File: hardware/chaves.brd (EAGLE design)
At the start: 100 x 100 mm, 80 parts, among them IC1 40106N

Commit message: all done except ground plane
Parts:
- removed E$1, E$2, E$3, E$4: (no value), holes:3,0
- removed R1, R2, R3, R4, R5, R6: 10k, adafruit:0204/7
- added IN1, IN2: WQP-PJ301M-12_JACK, MusicThingModular:WQP-PJ301M-12_JACK
- added JP6, JP7: (no value), adafruit:1X03-CLEANBIG
- added POT7, POT8: 10k, pot-alps:ALPS_POT_VERTICAL
- moved BJ 61.3 mm to (97.5, 15.0), turned to 180 degrees
- moved GJ 55.6 mm to (97.5, 19.5), turned to 180 degrees
- moved RJ 49.4 mm to (97.5, 24.5), turned to 180 degrees
- moved JHSYNC 45.6 mm to (97.5, 38.0)
- moved JVSYNC 43.9 mm to (97.5, 42.5)
- moved JGND 41.1 mm to (97.5, 29.0), turned to 90 degrees
- moved JVCC 35.1 mm to (97.5, 33.0), turned to 90 degrees
- moved JP2 32.3 mm to (71.5, 39.0)
- moved JP1 32.2 mm to (66.0, 39.0)
- moved IC1 14.3 mm to (66.5, 15.5), turned to 90 degrees
- moved C1 12.0 mm to (22.5, 87.0)
- moved C4 11.5 mm to (22.5, 72.0)
- moved C6 11.5 mm to (22.5, 58.0)
- moved C8 11.3 mm to (22.5, 45.0)
- moved C10 11.0 mm to (22.5, 30.5)
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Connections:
- removed net N$3 (its old number): C5.1, U$8.1
- removed net N$36: IC1.13, LDR2.1, POT6.P$1, POT6.P$2, U$12.2
- removed net N$6 (its old number): C6.1, U$9.3
- new net N$23: IN1.P$1_TIP, POT7.P$3
- new net N$46: C10.2, U$11.1
- new net N$47: C10.1, C11.1, IC1.11, POT5.P$1, POT5.P$2
- new net N$48: C11.2, U$11.3
- new net N$49: C13.2, U$12.3
- new net N$50: C12.2, U$12.1
- new net N$51: C12.1, C13.1, IC1.13, POT6.P$1, POT6.P$2
- net GND: now also IN1.P$3_SLEEVE, IN2.P$3_SLEEVE, POT7.P$1, POT8.P$1; no longer R1.1, R2.1, R3.1, R4.1, R5.1, R6.1
- net N$1: now also C1.2; no longer C2.1
- net N$10: now also C6.2, U$9.1; no longer C10.1, U$11.3
- net N$11: now also C7.2, U$9.3; no longer C13.1, U$12.1
- net N$12: now also JP6.1, JP6.2, JP6.3, POT7.P$2; no longer C12.1, U$12.3
- net N$18: no longer R1.2
- net N$19: now also LDR1.1
- net N$2: now also C2.2; no longer C1.1
- net N$22: now also LDR2.1
- net N$27: no longer R2.2
- net N$30: no longer R3.2
- net N$31: now also C1.1, C2.1; no longer LDR1.1, U$7.2
- net N$32: now also C4.1, C5.1; no longer U$8.2
- net N$33: now also C6.1, C7.1; no longer U$9.2
- net N$34: now also C8.1, C9.1; no longer U$10.2
- net N$35: now also JP7.1, JP7.3, POT8.P$2; no longer IC1.11, POT5.P$1, POT5.P$2, U$11.2
- net N$39: no longer R4.2
- net N$4: now also C5.2; no longer C4.1
- net N$42: no longer R5.2
- net N$45: no longer R6.2
- net N$5: now also C4.2, U$8.1; no longer C7.1, U$9.1
- net N$7: now also C8.2; no longer C9.1
- net N$8: now also C9.2; no longer C8.1
- net N$9: now also IN2.P$1_TIP, POT8.P$3; no longer C11.1, U$11.1
- net SS1: now also U$7.2; no longer C1.2, C2.2
- net SS2: now also U$8.2; no longer C4.2, C5.2
- net SS3: now also U$9.2; no longer C6.2, C7.2
- net SS4: now also U$10.2; no longer C8.2, C9.2
- net SS5: now also U$11.2; no longer C10.2, C11.2
- net SS6: now also U$12.2; no longer C12.2, C13.2
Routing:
- net N$36: track 75.9 -> 0.00 mm, vias 2 -> 0
- net N$14: track 82.1 -> 12.5 mm
- net N$13: track 77.6 -> 12.5 mm, vias 1 -> 0
- net N$39: track 84.5 -> 22.3 mm, vias 1 -> 0
- net N$30: track 93.6 -> 34.3 mm, vias 1 -> 0
- net N$47: track 0.00 -> 57.9 mm
- net N$32: track 87.3 -> 144.4 mm, vias 2 -> 0
- net N$51: track 0.00 -> 48.3 mm
- net N$15: track 59.3 -> 12.5 mm
- net N$20: track 60.8 -> 15.5 mm
- net N$21: track 56.4 -> 15.2 mm, vias 1 -> 0
- net N$18: track 111.2 -> 71.6 mm
- net N$27: track 100.7 -> 64.5 mm, vias 1 -> 0
- net GND: track 269.1 -> 302.8 mm, vias 2 -> 0
- net N$35: track 63.9 -> 30.5 mm, vias 0 -> 1
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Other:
- board text removed: "more information at github.com/Ttreintaysiete/chaves"

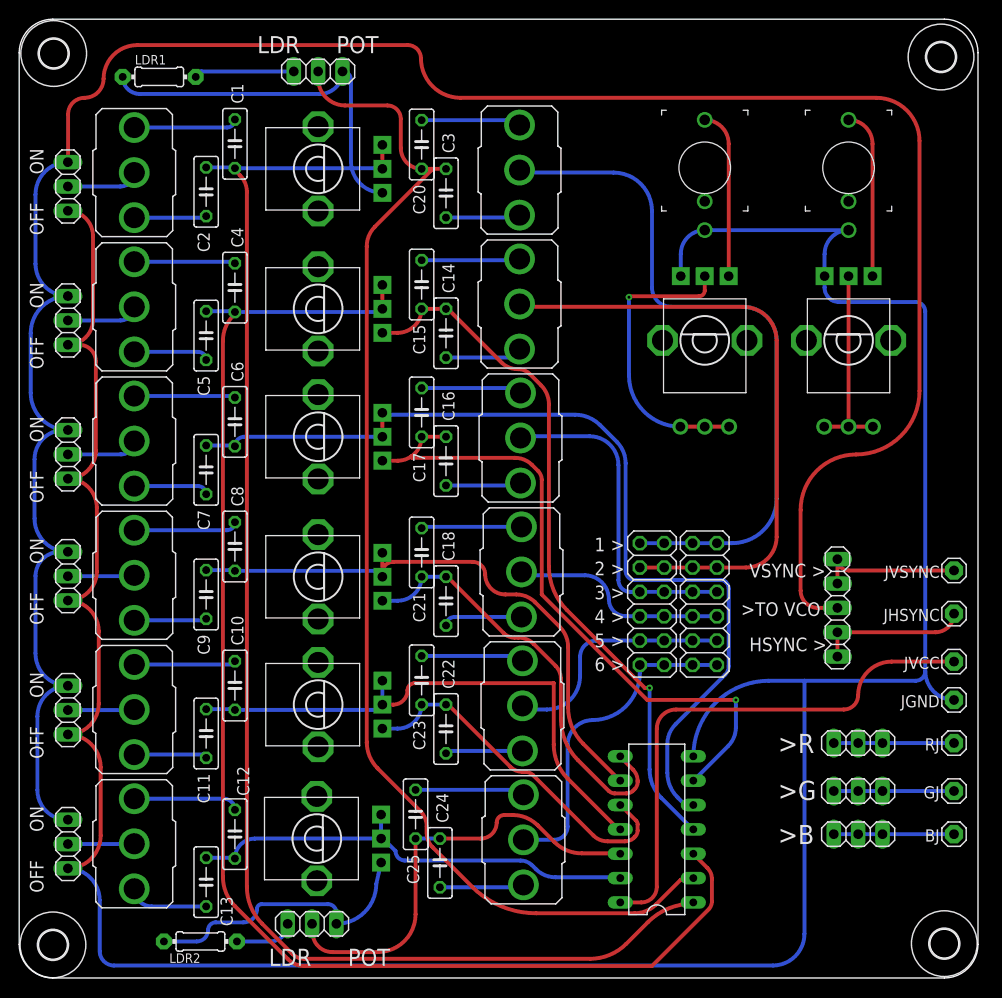
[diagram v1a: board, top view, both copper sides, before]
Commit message: Ground planed
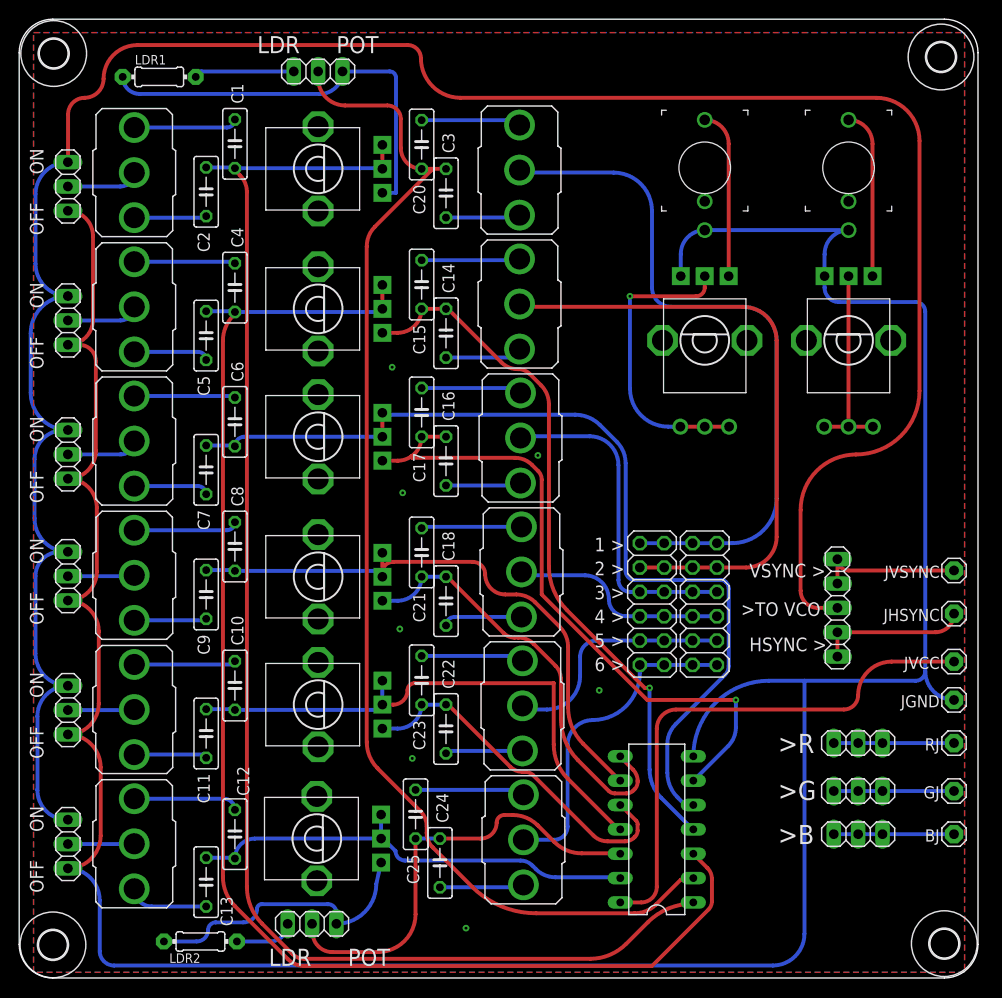
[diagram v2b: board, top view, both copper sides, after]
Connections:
- removed net N$35: JP7.1, JP7.3, POT8.P$2
- new net N$25: JP7.1, JP7.2, JP7.3, POT8.P$2
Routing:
- net N$25: track 0.00 -> 31.0 mm, vias 0 -> 1
- net N$35: track 30.5 -> 0.00 mm, vias 1 -> 0
- net N$19: track 39.0 -> 43.9 mm
- net GND: vias 0 -> 7
- added copper zone on layer 1, net GND
- added copper zone on layer 16, net GND
